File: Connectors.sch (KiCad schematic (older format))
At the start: 3 parts, among them J2 POWER_IN, J3 DBG_UART, J4 Conn_01x16

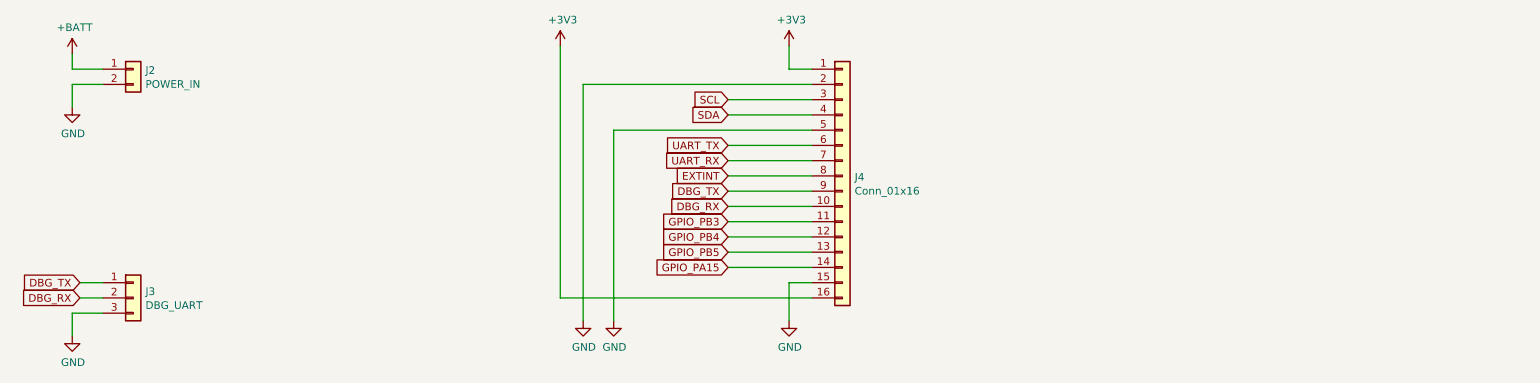
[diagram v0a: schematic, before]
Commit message: add jumper for power measurement; format GND a bit better
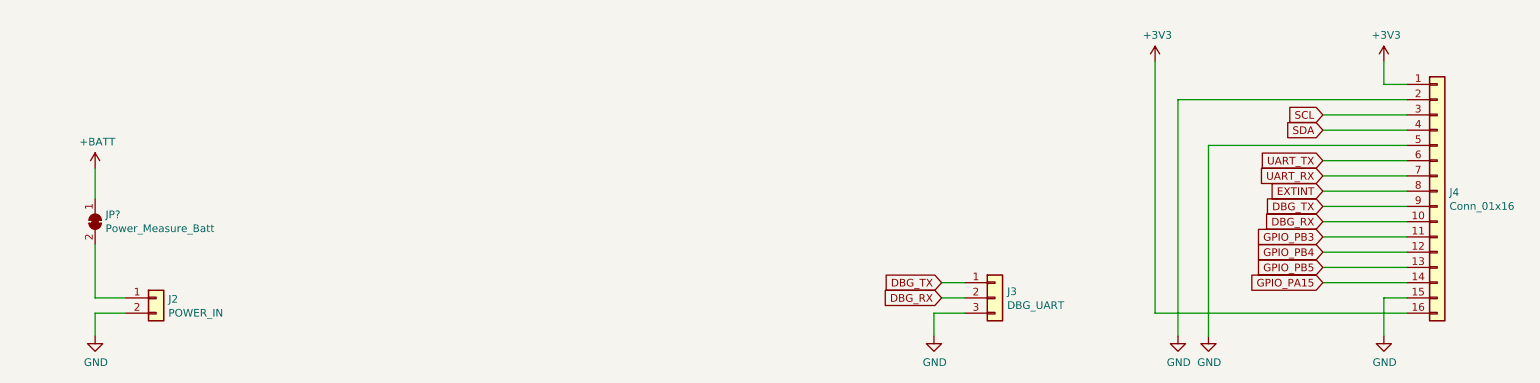
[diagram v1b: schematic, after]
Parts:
- added JP?: Power_Measure_Batt, symbol Jumper:SolderJumper_2_Bridged
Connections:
- net +BATT: now also JP?.1 (A); no longer J2.1 (Pin_1)
- new net: J2.1 (Pin_1), JP?.2 (B)
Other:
- moved on the sheet: J2, J3, J4
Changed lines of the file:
@@
 L Connector_Generic:Conn_01x02 J2
 U 1 1 5D179C38
-P 1700 1450
-F 0 "J2" H 1780 1442 50  0000 L CNN
-F 1 "POWER_IN" H 1780 1351 50  0000 L CNN
-F 2 "Connector_PinHeader_2.54mm:PinHeader_1x02_P2.54mm_Vertical" H 1700 1450 50  0001 C CNN
-F 3 "~" H 1700 1450 50  0001 C CNN
-	1    1700 1450
-	1    0    0    -1
-$EndComp
-$Comp
-L power:+BATT #PWR0130
-U 1 1 5D179C3E
-P 1300 1350
-F 0 "#PWR0130" H 1300 1200 50  0001 C CNN
-F 1 "+BATT" H 1315 1523 50  0000 C CNN
-F 2 "" H 1300 1350 50  0001 C CNN
-F 3 "" H 1300 1350 50  0001 C CNN
-	1    1300 1350
-	1    0    0    -1
-$EndComp
-Wire Wire Line
-	1300 1700 1300 1550
-Wire Wire Line
-	1300 1550 1500 1550
-Wire Wire Line
-	1500 1450 1300 1450
-Wire Wire Line
-	1300 1450 1300 1350
+P 1850 2950
+F 0 "J2" H 1930 2942 50  0000 L CNN
+F 1 "POWER_IN" H 1930 2851 50  0000 L CNN
+F 2 "Connector_PinHeader_2.54mm:PinHeader_1x02_P2.54mm_Vertical" H 1850 2950 50  0001 C CNN
+F 3 "~" H 1850 2950 50  0001 C CNN
+	1    1850 2950
+	1    0    0    -1
+$EndComp
+Wire Wire Line
+	1450 3200 1450 3050
+Wire Wire Line
+	1450 3050 1650 3050
+Wire Wire Line
+	1650 2950 1450 2950
 $Comp
 L power:+3V3 #PWR?
 U 1 1 5D1836DA
-P 6000 1300
+P 9900 1400
 AR Path="/5D1836DA" Ref="#PWR?"  Part="1"
 AR Path="/5D16888B/5D1836DA" Ref="#PWR0131"  Part="1"
-F 0 "#PWR0131" H 6000 1150 50  0001 C CNN
-F 1 "+3V3" H 6015 1473 50  0000 C CNN
-F 2 "" H 6000 1300 50  0001 C CNN
-F 3 "" H 6000 1300 50  0001 C CNN
-	1    6000 1300
-	1    0    0    -1
-$EndComp
-Wire Wire Line
-	6000 1300 6000 1450
-Wire Wire Line
-	6000 1450 6150 1450
+F 0 "#PWR0131" H 9900 1250 50  0001 C CNN
+F 1 "+3V3" H 9915 1573 50  0000 C CNN
+F 2 "" H 9900 1400 50  0001 C CNN
+F 3 "" H 9900 1400 50  0001 C CNN
+	1    9900 1400
+	1    0    0    -1
+$EndComp
+Wire Wire Line
+	9900 1400 9900 1550
+Wire Wire Line
+	9900 1550 10050 1550
 $Comp
 L power:GND #PWR?
 U 1 1 5D1836E6
-P 4650 3100
+P 8550 3200
 AR Path="/5D1836E6" Ref="#PWR?"  Part="1"
 AR Path="/5D16888B/5D1836E6" Ref="#PWR0132"  Part="1"
-F 0 "#PWR0132" H 4650 2850 50  0001 C CNN
-F 1 "GND" H 4655 2927 50  0000 C CNN
-F 2 "" H 4650 3100 50  0001 C CNN
-F 3 "" H 4650 3100 50  0001 C CNN
-	1    4650 3100
-	1    0    0    -1
-$EndComp
-Wire Wire Line
-	4650 1550 6150 1550
-Wire Wire Line
-	6150 1650 5600 1650
-Wire Wire Line
-	5600 1750 6150 1750
-Wire Wire Line
-	6150 1950 5600 1950
-Wire Wire Line
-	5600 2050 6150 2050
-Text GLabel 5600 1750 0    50   Input ~ 0
+F 0 "#PWR0132" H 8550 2950 50  0001 C CNN
+F 1 "GND" H 8555 3027 50  0000 C CNN
+F 2 "" H 8550 3200 50  0001 C CNN
+F 3 "" H 8550 3200 50  0001 C CNN
+	1    8550 3200
+	1    0    0    -1
+$EndComp
+Wire Wire Line
+	8550 1650 10050 1650
+Wire Wire Line
+	10050 1750 9500 1750
+Wire Wire Line
+	9500 1850 10050 1850
+Wire Wire Line
+	10050 2050 9500 2050
+Wire Wire Line
+	9500 2150 10050 2150
+Text GLabel 9500 1850 0    50   Input ~ 0
 SDA
-Text GLabel 5600 1650 0    50   Input ~ 0
+Text GLabel 9500 1750 0    50   Input ~ 0
 SCL
-Text GLabel 5600 1950 0    50   Input ~ 0
+Text GLabel 9500 2050 0    50   Input ~ 0
 UART_TX
-Text GLabel 5600 2050 0    50   Input ~ 0
+Text GLabel 9500 2150 0    50   Input ~ 0
 UART_RX
-Text GLabel 5600 2150 0    50   Input ~ 0
+Text GLabel 9500 2250 0    50   Input ~ 0
 EXTINT
-Text GLabel 5600 2250 0    50   Input ~ 0
+Text GLabel 9500 2350 0    50   Input ~ 0
 DBG_TX
-Text GLabel 5600 2350 0    50   Input ~ 0
+Text GLabel 9500 2450 0    50   Input ~ 0
 DBG_RX
-Text GLabel 5600 2450 0    50   Input ~ 0
+Text GLabel 9500 2550 0    50   Input ~ 0
 GPIO_PB3
-Text GLabel 5600 2550 0    50   Input ~ 0
+Text GLabel 9500 2650 0    50   Input ~ 0
 GPIO_PB4
-Text GLabel 5600 2650 0    50   Input ~ 0
+Text GLabel 9500 2750 0    50   Input ~ 0
 GPIO_PB5
-Text GLabel 5600 2750 0    50   Input ~ 0
+Text GLabel 9500 2850 0    50   Input ~ 0
 GPIO_PA15
 Wire Wire Line
-	4650 1550 4650 3100
+	8550 1650 8550 3200
 $Comp
 L power:GND #PWR?
 U 1 1 5D1D4F2A
-P 4850 3100
+P 8750 3200
 AR Path="/5D1D4F2A" Ref="#PWR?"  Part="1"
 AR Path="/5D16888B/5D1D4F2A" Ref="#PWR0133"  Part="1"
-F 0 "#PWR0133" H 4850 2850 50  0001 C CNN
-F 1 "GND" H 4855 2927 50  0000 C CNN
-F 2 "" H 4850 3100 50  0001 C CNN
-F 3 "" H 4850 3100 50  0001 C CNN
-	1    4850 3100
-	1    0    0    -1
-$EndComp
-Wire Wire Line
-	4850 3100 4850 1850
-Wire Wire Line
-	4850 1850 6150 1850
-Wire Wire Line
-	6150 2150 5600 2150
+F 0 "#PWR0133" H 8750 2950 50  0001 C CNN
+F 1 "GND" H 8755 3027 50  0000 C CNN
+F 2 "" H 8750 3200 50  0001 C CNN
+F 3 "" H 8750 3200 50  0001 C CNN
+	1    8750 3200
+	1    0    0    -1
+$EndComp
+Wire Wire Line
+	8750 3200 8750 1950
+Wire Wire Line
+	8750 1950 10050 1950
+Wire Wire Line
+	10050 2250 9500 2250
 $Comp
 L Connector_Generic:Conn_01x16 J4
 U 1 1 5D1D5844
-P 6350 2150
-F 0 "J4" H 6430 2142 50  0000 L CNN
-F 1 "Conn_01x16" H 6430 2051 50  0000 L CNN
-F 2 "Connector_PinHeader_2.54mm:PinHeader_1x16_P2.54mm_Vertical" H 6350 2150 50  0001 C CNN
-F 3 "~" H 6350 2150 50  0001 C CNN
-	1    6350 2150
-	1    0    0    -1
-$EndComp
-Wire Wire Line
-	6150 2250 5600 2250
-Wire Wire Line
-	5600 2350 6150 2350
-Wire Wire Line
-	6150 2450 5600 2450
-Wire Wire Line
-	5600 2550 6150 2550
-Wire Wire Line
-	5600 2650 6150 2650
-Wire Wire Line
-	5600 2750 6150 2750
+P 10250 2250
+F 0 "J4" H 10330 2242 50  0000 L CNN
+F 1 "Conn_01x16" H 10330 2151 50  0000 L CNN
+F 2 "Connector_PinHeader_2.54mm:PinHeader_1x16_P2.54mm_Vertical" H 10250 2250 50  0001 C CNN
+F 3 "~" H 10250 2250 50  0001 C CNN
+	1    10250 2250
+	1    0    0    -1
+$EndComp
+Wire Wire Line
+	10050 2350 9500 2350
+Wire Wire Line
+	9500 2450 10050 2450
+Wire Wire Line
+	10050 2550 9500 2550
+Wire Wire Line
+	9500 2650 10050 2650
+Wire Wire Line
+	9500 2750 10050 2750
+Wire Wire Line
+	9500 2850 10050 2850
 $Comp
 L Connector_Generic:Conn_01x03 J3
 U 1 1 5D1D8915
-P 1700 2950
-F 0 "J3" H 1780 2992 50  0000 L CNN
-F 1 "DBG_UART" H 1780 2901 50  0000 L CNN
-F 2 "Connector_PinHeader_2.54mm:PinHeader_1x03_P2.54mm_Vertical" H 1700 2950 50  0001 C CNN
-F 3 "~" H 1700 2950 50  0001 C CNN
-	1    1700 2950
-	1    0    0    -1
-$EndComp
-Text GLabel 1350 2850 0    50   Input ~ 0
+P 7350 2950
+F 0 "J3" H 7430 2992 50  0000 L CNN
+F 1 "DBG_UART" H 7430 2901 50  0000 L CNN
+F 2 "Connector_PinHeader_2.54mm:PinHeader_1x03_P2.54mm_Vertical" H 7350 2950 50  0001 C CNN
+F 3 "~" H 7350 2950 50  0001 C CNN
+	1    7350 2950
+	1    0    0    -1
+$EndComp
+Text GLabel 7000 2850 0    50   Input ~ 0
 DBG_TX
-Text GLabel 1350 2950 0    50   Input ~ 0
+Text GLabel 7000 2950 0    50   Input ~ 0
 DBG_RX
 $Comp
 L power:GND #PWR0134
 U 1 1 5D179C44
-P 1300 1700
-F 0 "#PWR0134" H 1300 1450 50  0001 C CNN
-F 1 "GND" H 1305 1527 50  0000 C CNN
-F 2 "" H 1300 1700 50  0001 C CNN
-F 3 "" H 1300 1700 50  0001 C CNN
-	1    1300 1700
+P 1450 3200
+F 0 "#PWR0134" H 1450 2950 50  0001 C CNN
+F 1 "GND" H 1455 3027 50  0000 C CNN
+F 2 "" H 1450 3200 50  0001 C CNN
+F 3 "" H 1450 3200 50  0001 C CNN
+	1    1450 3200
 	1    0    0    -1
 $EndComp
@@
 L power:GND #PWR0135
 U 1 1 5D1D9207
-P 1300 3200
-F 0 "#PWR0135" H 1300 2950 50  0001 C CNN
-F 1 "GND" H 1305 3027 50  0000 C CNN
-F 2 "" H 1300 3200 50  0001 C CNN
-F 3 "" H 1300 3200 50  0001 C CNN
-	1    1300 3200
-	1    0    0    -1
-$EndComp
-Wire Wire Line
-	1300 3200 1300 3050
-Wire Wire Line
-	1300 3050 1500 3050
-Wire Wire Line
-	1500 2950 1350 2950
-Wire Wire Line
-	1350 2850 1500 2850
+P 6950 3200
+F 0 "#PWR0135" H 6950 2950 50  0001 C CNN
+F 1 "GND" H 6955 3027 50  0000 C CNN
+F 2 "" H 6950 3200 50  0001 C CNN
+F 3 "" H 6950 3200 50  0001 C CNN
+	1    6950 3200
+	1    0    0    -1
+$EndComp
+Wire Wire Line
+	6950 3200 6950 3050
+Wire Wire Line
+	6950 3050 7150 3050
+Wire Wire Line
+	7150 2950 7000 2950
+Wire Wire Line
+	7000 2850 7150 2850
 $Comp
 L power:+3V3 #PWR?
 U 1 1 5D220AE3
-P 4500 1300
+P 8400 1400
 AR Path="/5D220AE3" Ref="#PWR?"  Part="1"
 AR Path="/5D16888B/5D220AE3" Ref="#PWR0136"  Part="1"
-F 0 "#PWR0136" H 4500 1150 50  0001 C CNN
-F 1 "+3V3" H 4515 1473 50  0000 C CNN
-F 2 "" H 4500 1300 50  0001 C CNN
-F 3 "" H 4500 1300 50  0001 C CNN
-	1    4500 1300
-	1    0    0    -1
-$EndComp
-Wire Wire Line
-	4500 1300 4500 2950
-Wire Wire Line
-	4500 2950 6150 2950
+F 0 "#PWR0136" H 8400 1250 50  0001 C CNN
+F 1 "+3V3" H 8415 1573 50  0000 C CNN
+F 2 "" H 8400 1400 50  0001 C CNN
+F 3 "" H 8400 1400 50  0001 C CNN
+	1    8400 1400
+	1    0    0    -1
+$EndComp
+Wire Wire Line
+	8400 1400 8400 3050
+Wire Wire Line
+	8400 3050 10050 3050
 $Comp
 L power:GND #PWR?
 U 1 1 5D221442
-P 6000 3100
+P 9900 3200
 AR Path="/5D221442" Ref="#PWR?"  Part="1"
 AR Path="/5D16888B/5D221442" Ref="#PWR0137"  Part="1"
-F 0 "#PWR0137" H 6000 2850 50  0001 C CNN
-F 1 "GND" H 6005 2927 50  0000 C CNN
-F 2 "" H 6000 3100 50  0001 C CNN
-F 3 "" H 6000 3100 50  0001 C CNN
-	1    6000 3100
-	1    0    0    -1
-$EndComp
-Wire Wire Line
-	6000 3100 6000 2850
-Wire Wire Line
-	6000 2850 6150 2850
+F 0 "#PWR0137" H 9900 2950 50  0001 C CNN
+F 1 "GND" H 9905 3027 50  0000 C CNN
+F 2 "" H 9900 3200 50  0001 C CNN
+F 3 "" H 9900 3200 50  0001 C CNN
+	1    9900 3200
+	1    0    0    -1
+$EndComp
+Wire Wire Line
+	9900 3200 9900 2950
+Wire Wire Line
+	9900 2950 10050 2950
+$Comp
+L power:+BATT #PWR?
+U 1 1 5D1B82A2
+P 1450 2100
+F 0 "#PWR?" H 1450 1950 50  0001 C CNN
+F 1 "+BATT" H 1465 2273 50  0000 C CNN
+F 2 "" H 1450 2100 50  0001 C CNN
+F 3 "" H 1450 2100 50  0001 C CNN
+	1    1450 2100
+	1    0    0    -1
+$EndComp
+$Comp
+L Jumper:SolderJumper_2_Bridged JP?
+U 1 1 5D1B8927
+P 1450 2450
+F 0 "JP?" V 1404 2518 50  0000 L CNN
+F 1 "Power_Measure_Batt" V 1495 2518 50  0000 L CNN
+F 2 "" H 1450 2450 50  0001 C CNN
+F 3 "~" H 1450 2450 50  0001 C CNN
+	1    1450 2450
+	0    1    1    0
+$EndComp
+Wire Wire Line
+	1450 2300 1450 2100
+Wire Wire Line
+	1450 2600 1450 2950
 $EndSCHEMATC

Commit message: some more annotations
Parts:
- JP3: renamed from JP?; footprint (none) -> Jumper:SolderJumper-2_P1.3mm_Bridged_Pad1.0x1.5mm
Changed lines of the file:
@@
 	9900 2950 10050 2950
 $Comp
-L power:+BATT #PWR?
+L power:+BATT #PWR0139
 U 1 1 5D1B82A2
 P 1450 2100
-F 0 "#PWR?" H 1450 1950 50  0001 C CNN
+F 0 "#PWR0139" H 1450 1950 50  0001 C CNN
 F 1 "+BATT" H 1465 2273 50  0000 C CNN
 F 2 "" H 1450 2100 50  0001 C CNN
@@
 $EndComp
 $Comp
-L Jumper:SolderJumper_2_Bridged JP?
+L Jumper:SolderJumper_2_Bridged JP3
 U 1 1 5D1B8927
 P 1450 2450
-F 0 "JP?" V 1404 2518 50  0000 L CNN
+F 0 "JP3" V 1404 2518 50  0000 L CNN
 F 1 "Power_Measure_Batt" V 1495 2518 50  0000 L CNN
-F 2 "" H 1450 2450 50  0001 C CNN
+F 2 "Jumper:SolderJumper-2_P1.3mm_Bridged_Pad1.0x1.5mm" H 1450 2450 50  0001 C CNN
 F 3 "~" H 1450 2450 50  0001 C CNN
 	1    1450 2450

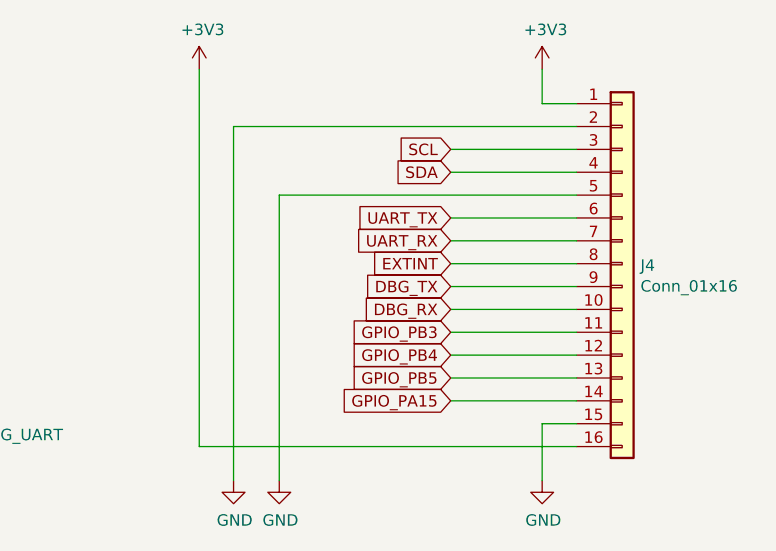
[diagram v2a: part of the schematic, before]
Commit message: add some wires
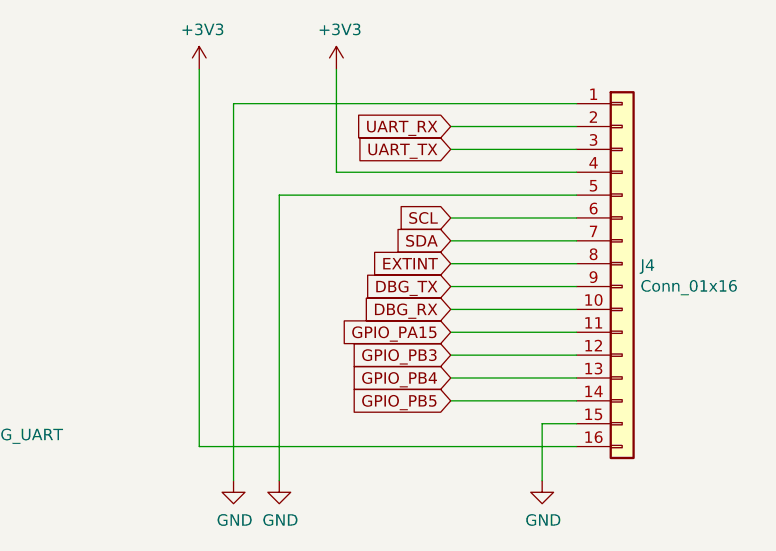
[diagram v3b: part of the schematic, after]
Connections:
- net +3V3: now also J4.4 (Pin_4); no longer J4.1 (Pin_1)
- net GND: now also J4.1 (Pin_1); no longer J4.2 (Pin_2)
- net GPIO_PA15: now also J4.11 (Pin_11); no longer J4.14 (Pin_14)
- net GPIO_PB3: now also J4.12 (Pin_12); no longer J4.11 (Pin_11)
- net GPIO_PB4: now also J4.13 (Pin_13); no longer J4.12 (Pin_12)
- net GPIO_PB5: now also J4.14 (Pin_14); no longer J4.13 (Pin_13)
- net SCL: now also J4.6 (Pin_6); no longer J4.3 (Pin_3)
- net SDA: now also J4.7 (Pin_7); no longer J4.4 (Pin_4)
- net UART_RX: now also J4.2 (Pin_2); no longer J4.7 (Pin_7)
- net UART_TX: now also J4.3 (Pin_3); no longer J4.6 (Pin_6)
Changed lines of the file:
@@
 L power:+3V3 #PWR?
 U 1 1 5D1836DA
-P 9900 1400
+P 9000 1400
 AR Path="/5D1836DA" Ref="#PWR?"  Part="1"
 AR Path="/5D16888B/5D1836DA" Ref="#PWR0131"  Part="1"
-F 0 "#PWR0131" H 9900 1250 50  0001 C CNN
-F 1 "+3V3" H 9915 1573 50  0000 C CNN
-F 2 "" H 9900 1400 50  0001 C CNN
-F 3 "" H 9900 1400 50  0001 C CNN
-	1    9900 1400
-	1    0    0    -1
-$EndComp
-Wire Wire Line
-	9900 1400 9900 1550
-Wire Wire Line
-	9900 1550 10050 1550
+F 0 "#PWR0131" H 9000 1250 50  0001 C CNN
+F 1 "+3V3" H 9015 1573 50  0000 C CNN
+F 2 "" H 9000 1400 50  0001 C CNN
+F 3 "" H 9000 1400 50  0001 C CNN
+	1    9000 1400
+	1    0    0    -1
+$EndComp
 $Comp
 L power:GND #PWR?
@@
 $EndComp
 Wire Wire Line
-	8550 1650 10050 1650
-Wire Wire Line
 	10050 1750 9500 1750
 Wire Wire Line
-	9500 1850 10050 1850
-Wire Wire Line
 	10050 2050 9500 2050
 Wire Wire Line
 	9500 2150 10050 2150
-Text GLabel 9500 1850 0    50   Input ~ 0
+Text GLabel 9500 2150 0    50   Input ~ 0
 SDA
+Text GLabel 9500 2050 0    50   Input ~ 0
+SCL
 Text GLabel 9500 1750 0    50   Input ~ 0
-SCL
-Text GLabel 9500 2050 0    50   Input ~ 0
 UART_TX
-Text GLabel 9500 2150 0    50   Input ~ 0
+Text GLabel 9500 1650 0    50   Input ~ 0
 UART_RX
 Text GLabel 9500 2250 0    50   Input ~ 0
@@
 Text GLabel 9500 2450 0    50   Input ~ 0
 DBG_RX
+Text GLabel 9500 2650 0    50   Input ~ 0
+GPIO_PB3
+Text GLabel 9500 2750 0    50   Input ~ 0
+GPIO_PB4
+Text GLabel 9500 2850 0    50   Input ~ 0
+GPIO_PB5
 Text GLabel 9500 2550 0    50   Input ~ 0
-GPIO_PB3
-Text GLabel 9500 2650 0    50   Input ~ 0
-GPIO_PB4
-Text GLabel 9500 2750 0    50   Input ~ 0
-GPIO_PB5
-Text GLabel 9500 2850 0    50   Input ~ 0
 GPIO_PA15
-Wire Wire Line
-	8550 1650 8550 3200
 $Comp
 L power:GND #PWR?
@@
 Wire Wire Line
 	1450 2600 1450 2950
+Wire Wire Line
+	9500 1650 10050 1650
+Wire Wire Line
+	9000 1400 9000 1850
+Wire Wire Line
+	9000 1850 10050 1850
+Wire Wire Line
+	8550 1550 8550 3200
+Wire Wire Line
+	8550 1550 10050 1550
 $EndSCHEMATC

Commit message: many optimizations; LAYOUT!
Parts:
- removed J4: Conn_01x16, Connector_PinHeader_2.54mm:PinHeader_1x16_P2.54mm_Vertical, symbol Connector_Generic:Conn_01x16
- added J4: Conn_01x14, Connector_PinHeader_2.54mm:PinHeader_1x14_P2.54mm_Vertical, symbol Connector_Generic:Conn_01x14
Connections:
- net +3V3: now also J4.14 (Pin_14), J4.4 (Pin_4)
- net EXTINT: now also J4.8 (Pin_8)
- net GND: now also J4.1 (Pin_1), J4.13 (Pin_13), J4.5 (Pin_5)
- net GPIO_PA15: now also J4.9 (Pin_9)
- net GPIO_PB3: now also J4.10 (Pin_10)
- net GPIO_PB4: now also J4.11 (Pin_11)
- net GPIO_PB5: now also J4.12 (Pin_12)
- net SCL: now also J4.6 (Pin_6)
- net SDA: now also J4.7 (Pin_7)
- net UART_RX: now also J4.2 (Pin_2)
- net UART_TX: now also J4.3 (Pin_3)
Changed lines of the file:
@@
 Text GLabel 9500 2250 0    50   Input ~ 0
 EXTINT
+Text GLabel 9500 2450 0    50   Input ~ 0
+GPIO_PB3
+Text GLabel 9500 2550 0    50   Input ~ 0
+GPIO_PB4
+Text GLabel 9500 2650 0    50   Input ~ 0
+GPIO_PB5
 Text GLabel 9500 2350 0    50   Input ~ 0
-DBG_TX
-Text GLabel 9500 2450 0    50   Input ~ 0
-DBG_RX
-Text GLabel 9500 2650 0    50   Input ~ 0
-GPIO_PB3
-Text GLabel 9500 2750 0    50   Input ~ 0
-GPIO_PB4
-Text GLabel 9500 2850 0    50   Input ~ 0
-GPIO_PB5
-Text GLabel 9500 2550 0    50   Input ~ 0
 GPIO_PA15
 $Comp
@@
 Wire Wire Line
 	10050 2250 9500 2250
-$Comp
-L Connector_Generic:Conn_01x16 J4
-U 1 1 5D1D5844
-P 10250 2250
-F 0 "J4" H 10330 2242 50  0000 L CNN
-F 1 "Conn_01x16" H 10330 2151 50  0000 L CNN
-F 2 "Connector_PinHeader_2.54mm:PinHeader_1x16_P2.54mm_Vertical" H 10250 2250 50  0001 C CNN
-F 3 "~" H 10250 2250 50  0001 C CNN
-	1    10250 2250
-	1    0    0    -1
-$EndComp
 Wire Wire Line
 	10050 2350 9500 2350
@@
 	9500 2450 10050 2450
 Wire Wire Line
-	10050 2550 9500 2550
+	9500 2550 10050 2550
 Wire Wire Line
 	9500 2650 10050 2650
-Wire Wire Line
-	9500 2750 10050 2750
-Wire Wire Line
-	9500 2850 10050 2850
 $Comp
 L Connector_Generic:Conn_01x03 J3
@@
 $EndComp
 Wire Wire Line
-	8400 1400 8400 3050
-Wire Wire Line
-	8400 3050 10050 3050
+	8400 1400 8400 2850
 $Comp
 L power:GND #PWR?
@@
 	1    0    0    -1
 $EndComp
-Wire Wire Line
-	9900 3200 9900 2950
-Wire Wire Line
-	9900 2950 10050 2950
 $Comp
 L power:+BATT #PWR0139
@@
 Wire Wire Line
 	8550 1550 10050 1550
+$Comp
+L Connector_Generic:Conn_01x14 J4
+U 1 1 5D1C10C6
+P 10250 2150
+F 0 "J4" H 10330 2142 50  0000 L CNN
+F 1 "Conn_01x14" H 10330 2051 50  0000 L CNN
+F 2 "Connector_PinHeader_2.54mm:PinHeader_1x14_P2.54mm_Vertical" H 10250 2150 50  0001 C CNN
+F 3 "~" H 10250 2150 50  0001 C CNN
+	1    10250 2150
+	1    0    0    -1
+$EndComp
+Wire Wire Line
+	10050 2750 9900 2750
+Wire Wire Line
+	10050 2850 8400 2850
+Wire Wire Line
+	9900 2750 9900 3200
 $EndSCHEMATC
